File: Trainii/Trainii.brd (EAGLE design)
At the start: 50.8 x 71.1 mm, 41 parts, among them J1 APDS-9960, J2 Left Mtr Encoder, J3 Right Mtr Encoder, J4 Line Sensor 1, J5 Line Sensor 2, J6 Ultrasonic, J7 Left Motor, J8 Right Motor, J9 Lift Motor, M1 ESP32, T1 MCH3383SC-70FL, T2 MCH3383SC-70FL, T3 MCH3383SC-70FL, U1 TPS61222DCKR, U2 BSS138, X1 JST-PH2

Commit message: Design Review Changes
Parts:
- removed R10, R12, R8: 91Ω, rcl:M0805
- removed R11, R7, R9: 47Ω, rcl:M0805
- R2, R3, R4: value 0.2Ω -> 10kΩ
- R5: value 10kΩ -> 47Ω; device rcl:R0805 -> rcl:M0805
- R6: value 10kΩ -> 91Ω; device rcl:R0805 -> rcl:M0805
- moved R4 63.3 mm to (10.2, 7.62), flipped to the top
- moved R3 36.9 mm to (26.7, 17.1), flipped to the top, turned to 180 degrees
- moved R2 35.6 mm to (13.3, 24.8), flipped to the top, turned to 270 degrees
- moved R5 17.1 mm to (10.2, 12.8), turned to 0 degrees
- moved J7 11.4 mm to (48.3, 50.2)
- moved C8 10.9 mm to (34.3, 30.5), flipped to the top, turned to 270 degrees
- moved R6 10.8 mm to (10.2, 18.4)
- moved C7 10.0 mm to (34.3, 52.1), flipped to the top, turned to 270 degrees
- moved J8 9.52 mm to (48.3, 61.6)
- moved C2 8.28 mm to (42.5, 52.1), flipped to the top, turned to 0 degrees
- moved J9 8.26 mm to (48.3, 34.3), turned to 90 degrees
- moved C4 3.24 mm to (42.5, 30.5), flipped to the top, turned to 0 degrees
- moved T1 2.54 mm to (43.2, 14.0), flipped to the top, turned to 0 degrees
- moved MC1 1.27 mm to (40.6, 56.5), flipped to the top, turned to 180 degrees
- moved MC2 1.27 mm to (40.6, 34.9), flipped to the top, turned to 180 degrees
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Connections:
- removed net LINE_OUT_1_3V3: M1.A2, R10.1, R9.2
- removed net LINE_OUT_1_5V: J4.3, R9.1
- removed net LINE_OUT_2_3V3: M1.A3, R11.2, R12.1
- removed net LINE_OUT_2_5V: J5.3, R11.1
- removed net N$10: MC1.3, R4.1
- removed net N$6: MC2.3, R2.2
- removed net N$9: MC1.6, R3.1
- new net LINE_OUT_1: J4.3, M1.A2
- new net LINE_OUT_2: J5.3, M1.A3
- net +5V: now also R4.1; no longer J4.2, J5.2, R6.1
- net 3V3: now also J4.2, J5.2, R2.2, R3.1; no longer R5.1
- net ECHO_3V3: now also M1.MI, R5.2, R6.1; no longer M1.A9, R7.2, R8.1
- net ECHO_5V: now also R5.1; no longer R7.1
- net GND: now also MC1.3, MC1.6, MC2.3, MC2.6, R6.2; no longer R10.2, R12.2, R2.1, R3.2, R4.2, R8.2
- net LEFT_B: now also M1.A10; no longer M1.A12
- net MOTOR_FAULT: now also R2.1
- net RIGHT_A: now also M1.A9; no longer M1.A10
- net TRIG_3V3: now also M1.MO, R3.2; no longer M1.A0, R5.2
- net TRIG_5V: now also R4.2; no longer R6.2
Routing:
- net +5V: track 73.1 -> 23.2 mm
- net MOTOR_FAULT: track 62.5 -> 84.8 mm
- net LINE_OUT_1_3V3: track 19.0 -> 0.00 mm, vias 1 -> 0
- net TRIG_3V3: track 51.8 -> 32.8 mm, vias 2 -> 1
- net GND: track 22.2 -> 41.0 mm, vias 1 -> 23
- net VBAT_MOTOR_FUSE: track 77.0 -> 94.8 mm, vias 2 -> 0
- net LINE_OUT_1: track 0.00 -> 13.9 mm
- net ECHO_3V3: track 37.0 -> 23.4 mm, vias 2 -> 1
- net LINE_OUT_2_3V3: track 11.1 -> 0.00 mm
- net RIGHT_A: track 18.7 -> 28.0 mm, vias 1 -> 0
- net LEFT_1: track 4.47 -> 13.4 mm
- net LINE_OUT_2_5V: track 8.57 -> 0.00 mm
- net LINE_OUT_1_5V: track 8.57 -> 0.00 mm
- net LINE_OUT_2: track 0.00 -> 6.66 mm
- net RIGHT_B: track 23.5 -> 29.7 mm, vias 1 -> 0
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
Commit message: A E S T H E T I C S
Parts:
- added U$2: (no value), RoboJackets-Aesthetics:ROBOJACKETS
- added U$6: (no value), RoboJackets-Aesthetics:ROBOBUZZ_0.4X
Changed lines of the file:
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@@
 <attribute name="SPICEPREFIX" value="R" x="13.335" y="24.765" size="1.778" layer="27" rot="R270" display="off"/>
 </element>
+<element name="U$2" library="RoboJackets-Aesthetics" package="ROBOJACKETS" value="" x="24.765" y="27.305" rot="R90"/>
+<element name="U$6" library="RoboJackets-Aesthetics" package="ROBOBUZZ_0.4X" value="" x="39.37" y="62.865"/>
 </elements>
 <signals>

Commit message: Moved robobuzz
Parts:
- moved U$6 1.90 mm to (37.5, 62.9)
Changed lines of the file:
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@@
 </element>
 <element name="U$2" library="RoboJackets-Aesthetics" package="ROBOJACKETS" value="" x="24.765" y="27.305" rot="R90"/>
-<element name="U$6" library="RoboJackets-Aesthetics" package="ROBOBUZZ_0.4X" value="" x="39.37" y="62.865"/>
+<element name="U$6" library="RoboJackets-Aesthetics" package="ROBOBUZZ_0.4X" value="" x="37.465" y="62.865"/>
 </elements>
 <signals>

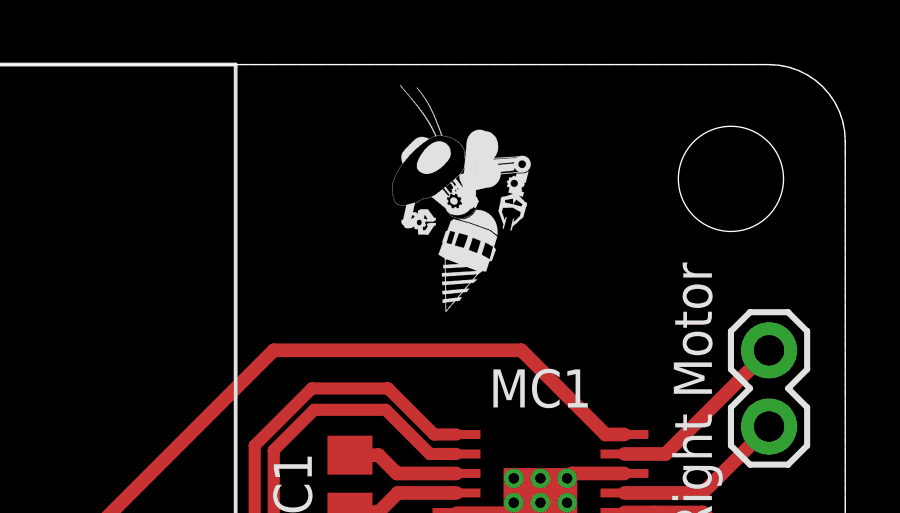
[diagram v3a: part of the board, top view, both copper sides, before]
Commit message: Added place for numbering, updated images and bom
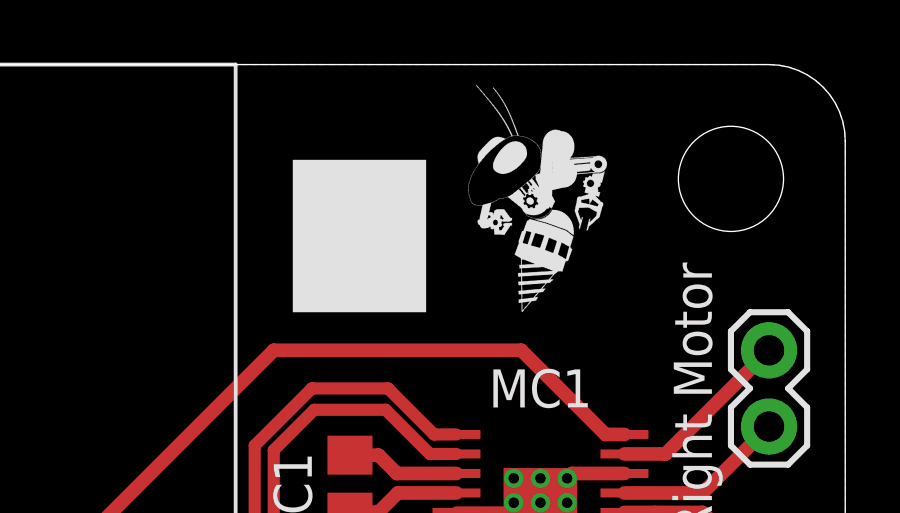
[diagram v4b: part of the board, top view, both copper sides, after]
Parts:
- moved U$6 2.54 mm to (40.0, 62.9)
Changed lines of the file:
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@@
 <text x="25.4" y="8.89" size="1.016" layer="21" font="vector" ratio="20" rot="R180">CHRG</text>
 <text x="34.925" y="8.89" size="1.016" layer="21" font="vector" ratio="20" rot="R180">RUN</text>
+<rectangle x1="32.385" y1="62.865" x2="36.83" y2="67.945" layer="21"/>
 </plain>
 <attributes>
@@
 </element>
 <element name="U$2" library="RoboJackets-Aesthetics" package="ROBOJACKETS" value="" x="24.765" y="27.305" rot="R90"/>
-<element name="U$6" library="RoboJackets-Aesthetics" package="ROBOBUZZ_0.4X" value="" x="37.465" y="62.865"/>
+<element name="U$6" library="RoboJackets-Aesthetics" package="ROBOBUZZ_0.4X" value="" x="40.005" y="62.865"/>
 </elements>
 <signals>

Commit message: Increase resistance to reduce current
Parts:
- R5: value 47Ω -> 2k2Ω
- R6: value 91Ω -> 4k3Ω
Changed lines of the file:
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@@
 <attribute name="VENDOR" value="Fairchild Semiconductor" x="26.67" y="11.43" size="1.778" layer="27" rot="R180" display="off"/>
 </element>
-<element name="R5" library="rcl" library_urn="urn:adsk.eagle:library:334" package="M0805" package3d_urn="urn:adsk.eagle:package:23556/1" value="47Ω" x="10.16" y="12.827" smashed="yes">
+<element name="R5" library="rcl" library_urn="urn:adsk.eagle:library:334" package="M0805" package3d_urn="urn:adsk.eagle:package:23556/1" value="2k2Ω" x="10.16" y="12.827" smashed="yes">
 <attribute name="NAME" x="10.16" y="14.605" size="1.27" layer="25" align="center"/>
 <attribute name="SPICEPREFIX" value="R" x="10.16" y="12.827" size="1.778" layer="27" display="off"/>
 </element>
-<element name="R6" library="rcl" library_urn="urn:adsk.eagle:library:334" package="M0805" package3d_urn="urn:adsk.eagle:package:23556/1" value="91Ω" x="10.16" y="18.415" smashed="yes">
+<element name="R6" library="rcl" library_urn="urn:adsk.eagle:library:334" package="M0805" package3d_urn="urn:adsk.eagle:package:23556/1" value="4k3Ω" x="10.16" y="18.415" smashed="yes">
 <attribute name="NAME" x="10.16" y="16.51" size="1.27" layer="25" align="center"/>
 <attribute name="SPICEPREFIX" value="R" x="10.16" y="18.415" size="1.778" layer="27" display="off"/>

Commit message: Adjusted small routes
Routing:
- net 3V3: track 113.5 -> 118.7 mm
- net TRIG_3V3: track 32.8 -> 31.7 mm
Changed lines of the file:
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@@
 <contactref element="M1" pad="22"/>
 <wire x1="29.21" y1="29.21" x2="39.37" y2="19.05" width="0.4064" layer="16"/>
+<wire x1="45.72" y1="19.05" x2="46.99" y2="17.78" width="0.4064" layer="1"/>
 <via x="39.37" y="19.05" extent="1-16" drill="0.35"/>
-<wire x1="45.72" y1="19.05" x2="46.99" y2="17.78" width="0.4064" layer="1"/>
 <wire x1="39.37" y1="19.05" x2="45.72" y2="19.05" width="0.4064" layer="1"/>
 </signal>
@@
 <wire x1="29.21" y1="26.67" x2="30.48" y2="26.67" width="0.4064" layer="16"/>
 <wire x1="30.48" y1="26.67" x2="38.735" y2="18.415" width="0.4064" layer="16"/>
-<wire x1="38.735" y1="18.415" x2="38.8084" y2="18.415" width="0.4064" layer="16"/>
-<via x="38.8084" y="18.415" extent="1-16" drill="0.35"/>
-<wire x1="38.8084" y1="18.415" x2="38.8564" y2="18.367" width="0.4064" layer="1"/>
-<wire x1="43.863" y1="18.367" x2="46.99" y2="15.24" width="0.4064" layer="1"/>
-<wire x1="38.8564" y1="18.367" x2="43.863" y2="18.367" width="0.4064" layer="1"/>
+<wire x1="45.085" y1="17.145" x2="46.99" y2="15.24" width="0.4064" layer="1"/>
+<wire x1="38.735" y1="18.415" x2="39.37" y2="17.78" width="0.4064" layer="16"/>
+<via x="39.37" y="17.78" extent="1-16" drill="0.35"/>
+<wire x1="39.37" y1="17.78" x2="44.45" y2="17.78" width="0.4064" layer="1"/>
+<wire x1="44.45" y1="17.78" x2="45.085" y2="17.145" width="0.4064" layer="1"/>
 </signal>
 <signal name="TICK_LEFT">
@@
 <wire x1="3.81" y1="58.42" x2="1.27" y2="55.88" width="0.4064" layer="1"/>
 <wire x1="1.27" y1="55.88" x2="1.27" y2="50.8" width="0.4064" layer="1"/>
-<wire x1="31.115" y1="17.145" x2="38.735" y2="17.145" width="0.4064" layer="16"/>
-<wire x1="38.735" y1="17.145" x2="46.99" y2="25.4" width="0.4064" layer="16"/>
+<wire x1="38.735" y1="17.145" x2="35.56" y2="17.145" width="0.4064" layer="16"/>
+<wire x1="35.56" y1="17.145" x2="31.115" y2="17.145" width="0.4064" layer="16"/>
 <wire x1="20.32" y1="13.6121" x2="20.32" y2="12.065" width="0.4064" layer="1"/>
 <wire x1="20.989" y1="11.396" x2="20.989" y2="8.763" width="0.4064" layer="1"/>
@@
 <wire x1="3.81" y1="48.26" x2="1.27" y2="50.8" width="0.4064" layer="1"/>
 <wire x1="8.89" y1="62.23" x2="5.08" y2="58.42" width="0.4064" layer="1"/>
+<wire x1="35.56" y1="17.145" x2="38.735" y2="17.145" width="0.4064" layer="16"/>
+<wire x1="38.735" y1="17.145" x2="39.37" y2="16.51" width="0.4064" layer="16"/>
+<wire x1="39.37" y1="16.51" x2="40.64" y2="16.51" width="0.4064" layer="16"/>
+<wire x1="41.275" y1="17.145" x2="40.64" y2="16.51" width="0.4064" layer="16"/>
+<wire x1="46.99" y1="25.4" x2="41.275" y2="19.685" width="0.4064" layer="16"/>
+<wire x1="41.275" y1="19.685" x2="41.275" y2="17.145" width="0.4064" layer="16"/>
 </signal>
 <signal name="TICK_RIGHT">
@@
 <wire x1="24.13" y1="17.78" x2="24.765" y2="17.145" width="0.4064" layer="1"/>
 <wire x1="24.765" y1="17.145" x2="25.72" y2="17.145" width="0.4064" layer="1"/>
-<wire x1="24.13" y1="17.78" x2="24.13" y2="23.495" width="0.4064" layer="16"/>
+<wire x1="24.13" y1="19.685" x2="24.13" y2="17.78" width="0.4064" layer="16"/>
 <contactref element="M1" pad="MO"/>
-<wire x1="10.795" y1="36.83" x2="8.89" y2="36.83" width="0.4064" layer="16"/>
-<wire x1="24.13" y1="23.495" x2="10.795" y2="36.83" width="0.4064" layer="16"/>
+<wire x1="19.3675" y1="24.4475" x2="24.13" y2="19.685" width="0.4064" layer="16"/>
+<wire x1="8.89" y1="36.83" x2="19.3675" y2="26.3525" width="0.4064" layer="16"/>
+<wire x1="19.3675" y1="26.3525" x2="19.3675" y2="24.4475" width="0.4064" layer="16"/>
 </signal>
 <signal name="TRIG_5V">
@@
 <contactref element="T3" pad="2"/>
 <contactref element="F1" pad="1"/>
-<wire x1="38.1" y1="21.3614" x2="38.1" y2="15.5675" width="0.4572" layer="1"/>
-<wire x1="38.1" y1="15.5675" x2="37.7875" y2="15.255" width="0.4572" layer="1"/>
+<wire x1="37.7875" y1="15.255" x2="38.1" y2="15.5675" width="0.4572" layer="1"/>
+<wire x1="38.1" y1="15.5675" x2="38.1" y2="21.3614" width="0.4572" layer="1"/>
 </signal>
 <signal name="N$13">

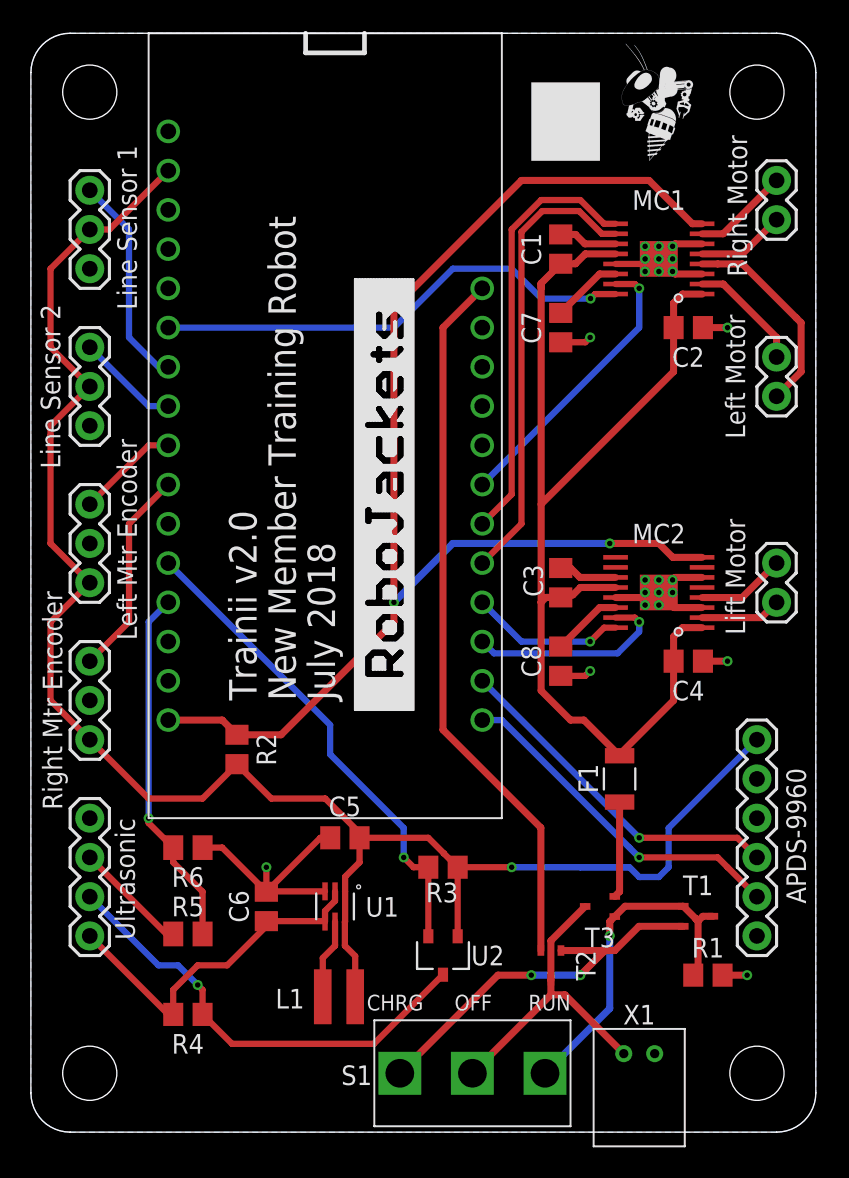
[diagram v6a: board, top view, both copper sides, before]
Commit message: Removed additional transistor to allow for charging to work correctly
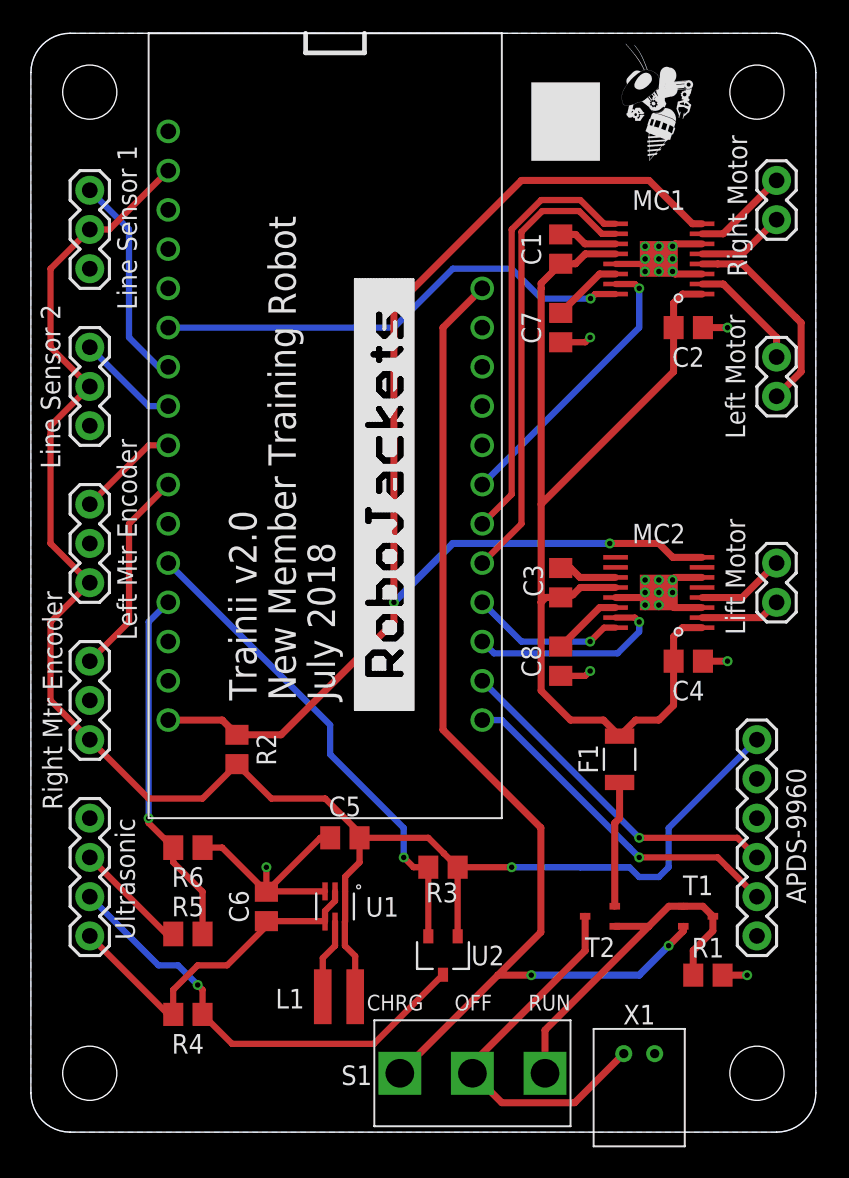
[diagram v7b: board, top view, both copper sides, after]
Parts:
- removed T3: MCH3383SC-70FL, Trainii:SOTFL65P210X90-3
- moved T2 4.49 mm to (36.8, 14.0), turned to 180 degrees
- moved F1 1.27 mm to (38.1, 24.1)
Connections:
- removed net N$13: R1.2, S1.3, T1.1, T1.3, T3.1
- removed net N$3: S1.1, T1.2, T2.1
- new net N$2: R1.2, S1.3, T1.1, T1.3, T2.1
- net VBAT: no longer T3.3
- net VBAT_HUZZAH: now also S1.1, T1.2; no longer T2.2
- net VBAT_MOTOR: now also T2.2; no longer T3.2
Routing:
- net N$3: track 25.4 -> 0.00 mm, vias 2 -> 0
- net VBAT_HUZZAH: track 46.5 -> 71.7 mm, vias 0 -> 2
- net N$2: track 0.00 -> 24.2 mm
- net N$13: track 23.0 -> 0.00 mm, vias 1 -> 0
- net VBAT: track 20.1 -> 25.1 mm
- net VBAT_MOTOR: track 6.24 -> 8.14 mm
- net VBAT_MOTOR_FUSE: track 94.8 -> 93.3 mm

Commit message: Added gerbers
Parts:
- moved R3 1.27 mm to (26.7, 15.9)
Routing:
- net 3V3: track 118.7 -> 113.6 mm
- net N$2: track 24.2 -> 22.9 mm
- net MOTOR_FAULT: track 84.8 -> 84.2 mm
- net GND: vias 23 -> 24
